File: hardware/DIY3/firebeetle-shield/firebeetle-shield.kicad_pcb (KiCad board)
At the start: 2 copper layers, 34 x 72 mm, 9 parts, among them J1 Conn_01x14_Female, J2 Conn_01x06_Female (DS3231), J3 Conn_01x04_Male (MS5803), J4 Conn_01x06_Female (microSD), J5 Conn_01x18_Female

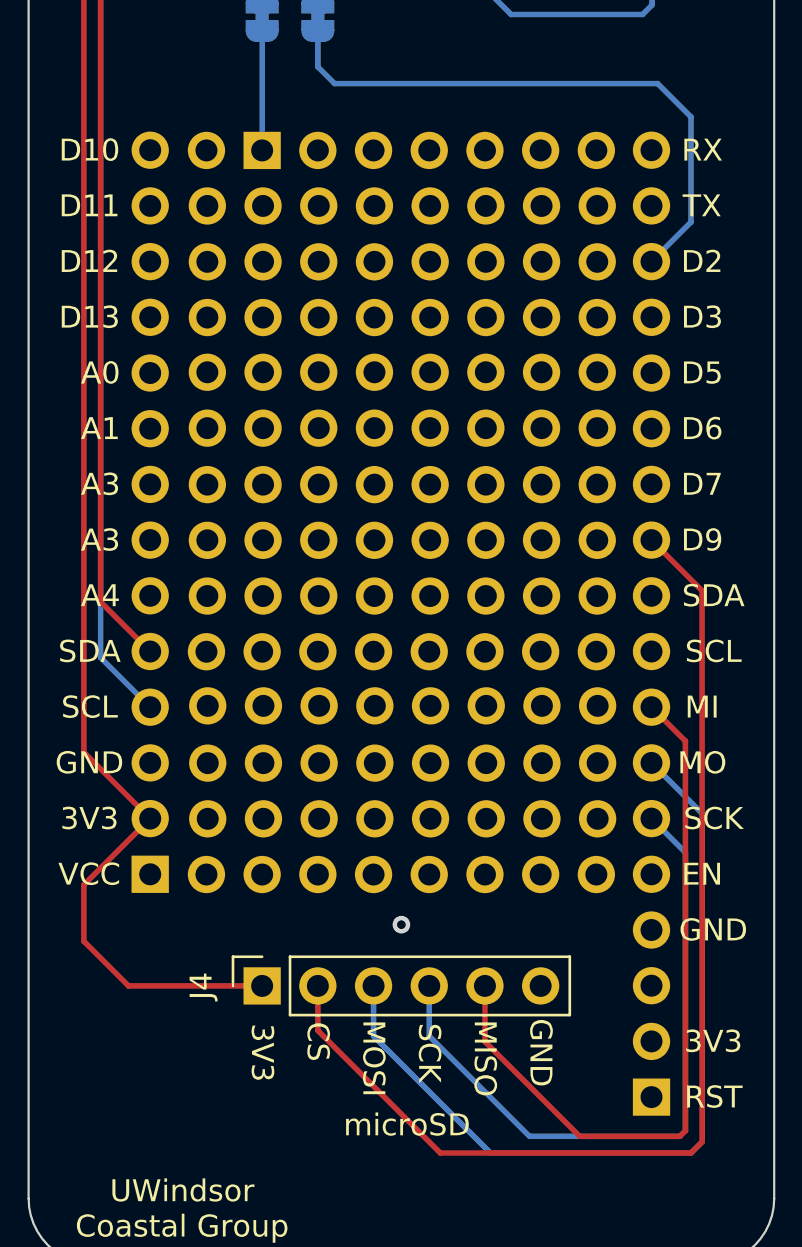
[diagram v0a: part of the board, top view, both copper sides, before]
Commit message: Fix schematic errors/conflicts and clean up
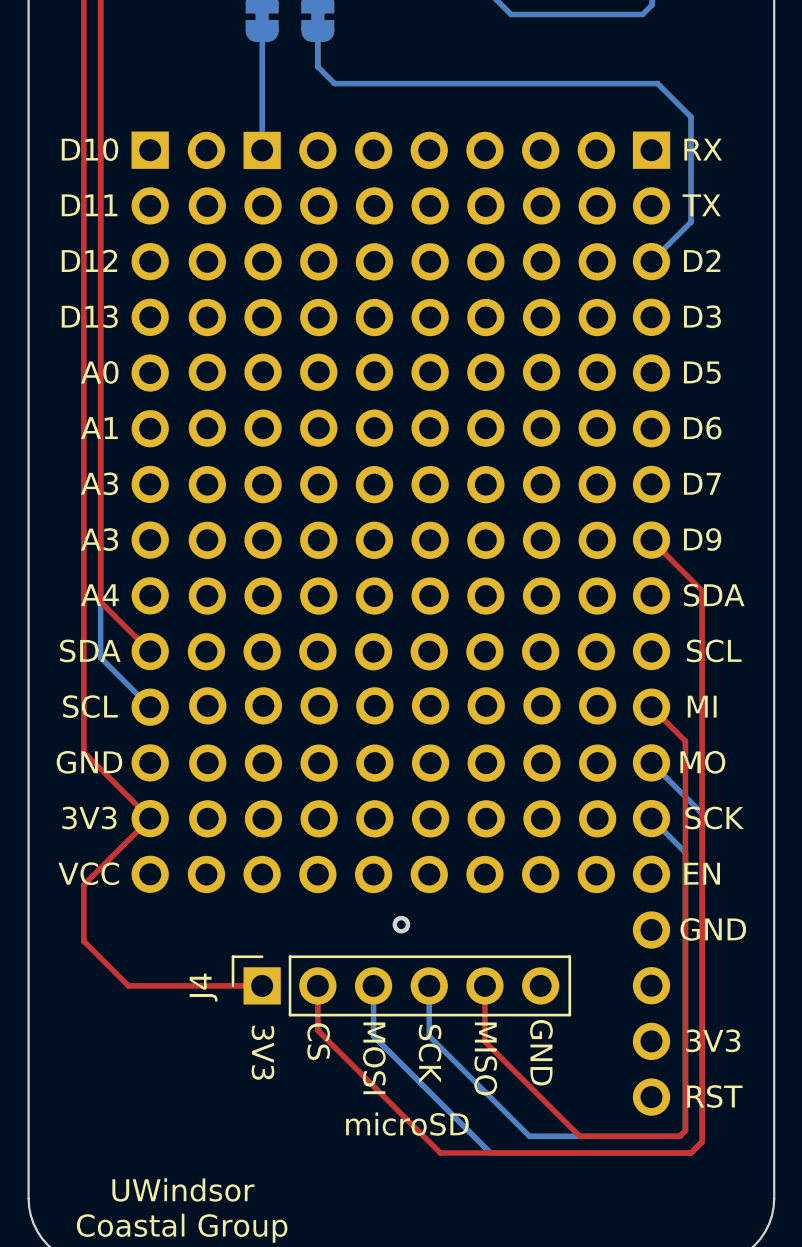
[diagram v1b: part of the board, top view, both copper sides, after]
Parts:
- J2: value Conn_01x06_Female (DS3231) -> Conn_01x06_Female
- J3: value Conn_01x04_Male (MS5803) -> Conn_01x04_Male
- J4: value Conn_01x06_Female (microSD) -> Conn_01x06_Female
- moved J5 43.2 mm to (126.4, 121.2), turned to 180 degrees
- moved J1 33.0 mm to (103.5, 121.2), turned to 180 degrees
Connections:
- J1 pad 1: VCC -> unconnected-(J1-Pad1)
- J1 pad 10: A0 -> SDA
- J1 pad 11: D13 -> SCL
- J1 pad 12: D12 -> GND
- J1 pad 13: D11 -> 3V3
- J1 pad 14: D10 -> VCC
- J1 pad 2: 3V3 -> unconnected-(J1-Pad2)
- J1 pad 3: GND -> unconnected-(J1-Pad3)
- J1 pad 4: SCL -> unconnected-(J1-Pad4)
- J1 pad 5: SDA -> unconnected-(J1-Pad5)
- J1 pad 6: A4 -> unconnected-(J1-Pad6)
- J1 pad 7: A3 -> unconnected-(J1-Pad7)
- J1 pad 8: A2 -> unconnected-(J1-Pad8)
- J1 pad 9: A1 -> unconnected-(J1-Pad9)
- J5 pad 1: RST -> unconnected-(J5-Pad1)
- J5 pad 10: SDA -> unconnected-(J5-Pad10)
- J5 pad 11: CS -> MISO
- J5 pad 12: D7 -> MOSI
- J5 pad 13: D6 -> SCK
- J5 pad 14: D5 -> unconnected-(J5-Pad14)
- J5 pad 15: D3 -> GND
- J5 pad 16: D2 -> unconnected-(J5-Pad16)
- J5 pad 17: TX -> unconnected-(J5-Pad17)
- J5 pad 18: RX -> unconnected-(J5-Pad18)
- J5 pad 2: 3V3 -> unconnected-(J5-Pad2)
- J5 pad 3: NONE -> SQW
- J5 pad 4: GND -> unconnected-(J5-Pad4)
- J5 pad 5: EN -> unconnected-(J5-Pad5)
- J5 pad 6: SCK -> unconnected-(J5-Pad6)
- J5 pad 7: MOSI -> unconnected-(J5-Pad7)
- J5 pad 8: MISO -> CS
- J5 pad 9: SCL -> unconnected-(J5-Pad9)
- JP2 pad 2: D2 -> SQW
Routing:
- net SQW: track 0.00 -> 26.9 mm
- net D2: track 26.9 -> 0.00 mm
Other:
- board text removed: "Notes for next iteration: - put shield header pin outline on front silkscreen - maybe change JST pin spacing to 2.54 mm instead of 2 mm - change {dblquote}UWindsor Coastal Group{dblquote} to {dblquote}Windsor Coastal Group{dblquote} and increase font size - include group logo RTC: - Connect DS3231 3V3 directly to D3, not main board's 3V3 - Include I2C pull up resistors - Maybe just include DS3231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"
